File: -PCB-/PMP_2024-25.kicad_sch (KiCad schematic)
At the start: 45 parts, among them J1 OUT, J2 5V, J3 GND, J4 CALIB, Q1 NPN 2N3904, Q2 NPN 2N3904, Q3 NPN MPSA42, Q4 NPN 2N3904

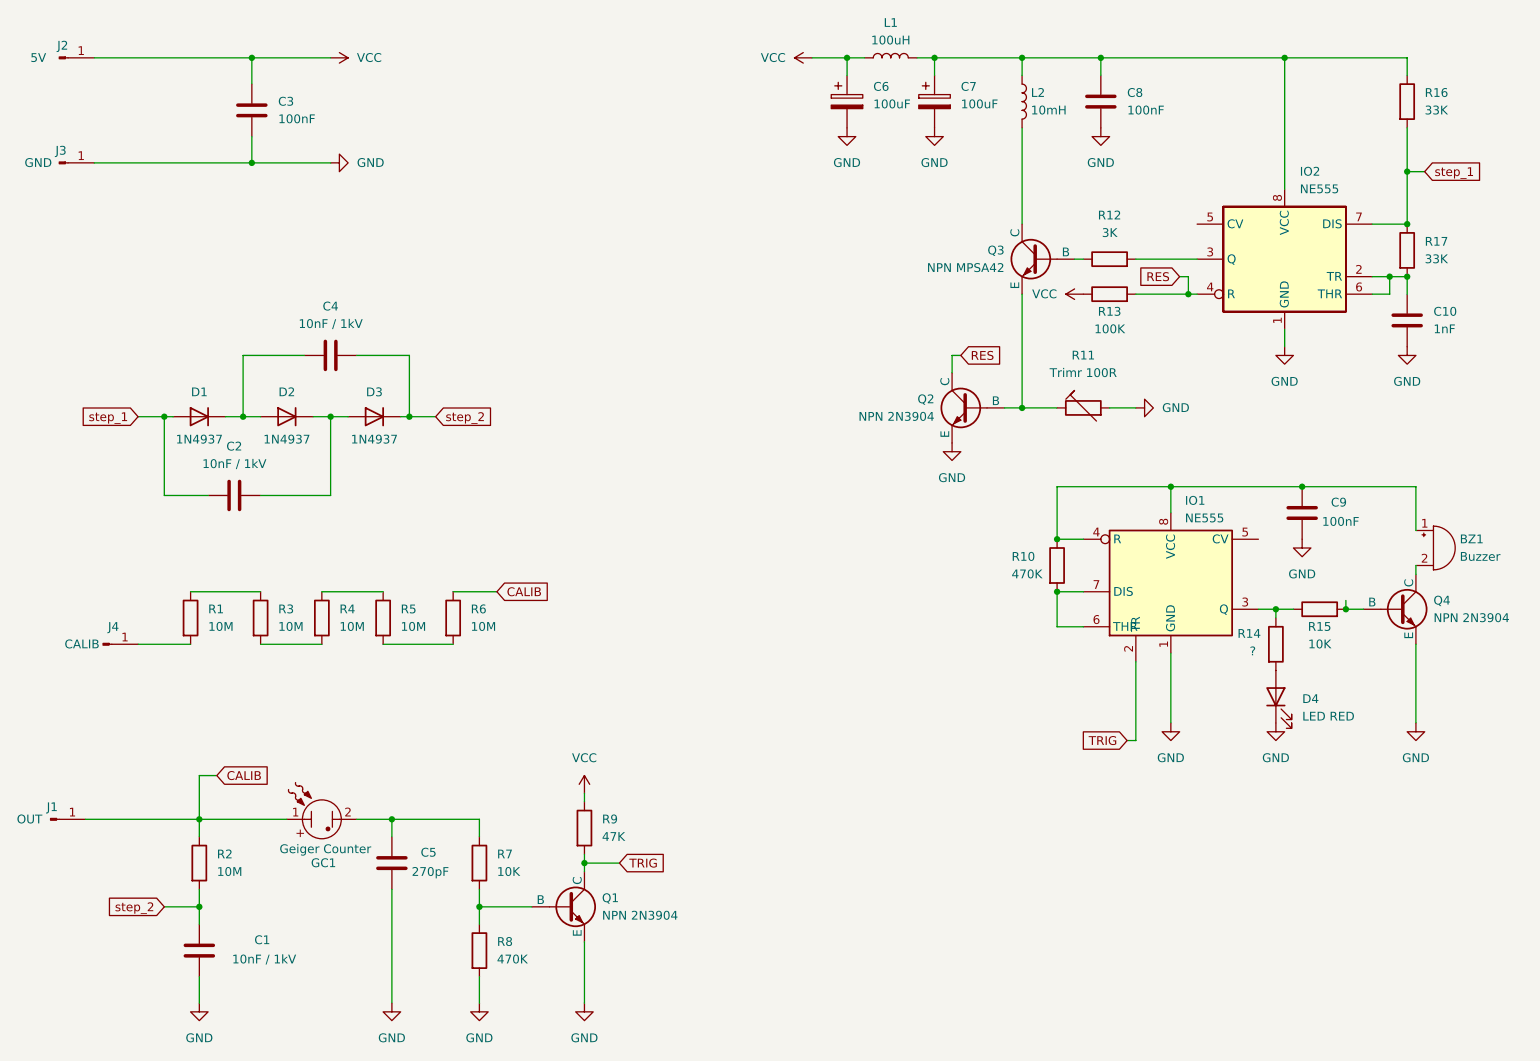
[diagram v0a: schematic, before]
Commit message: schematic update
odebrany chyby, pridany krizky apod
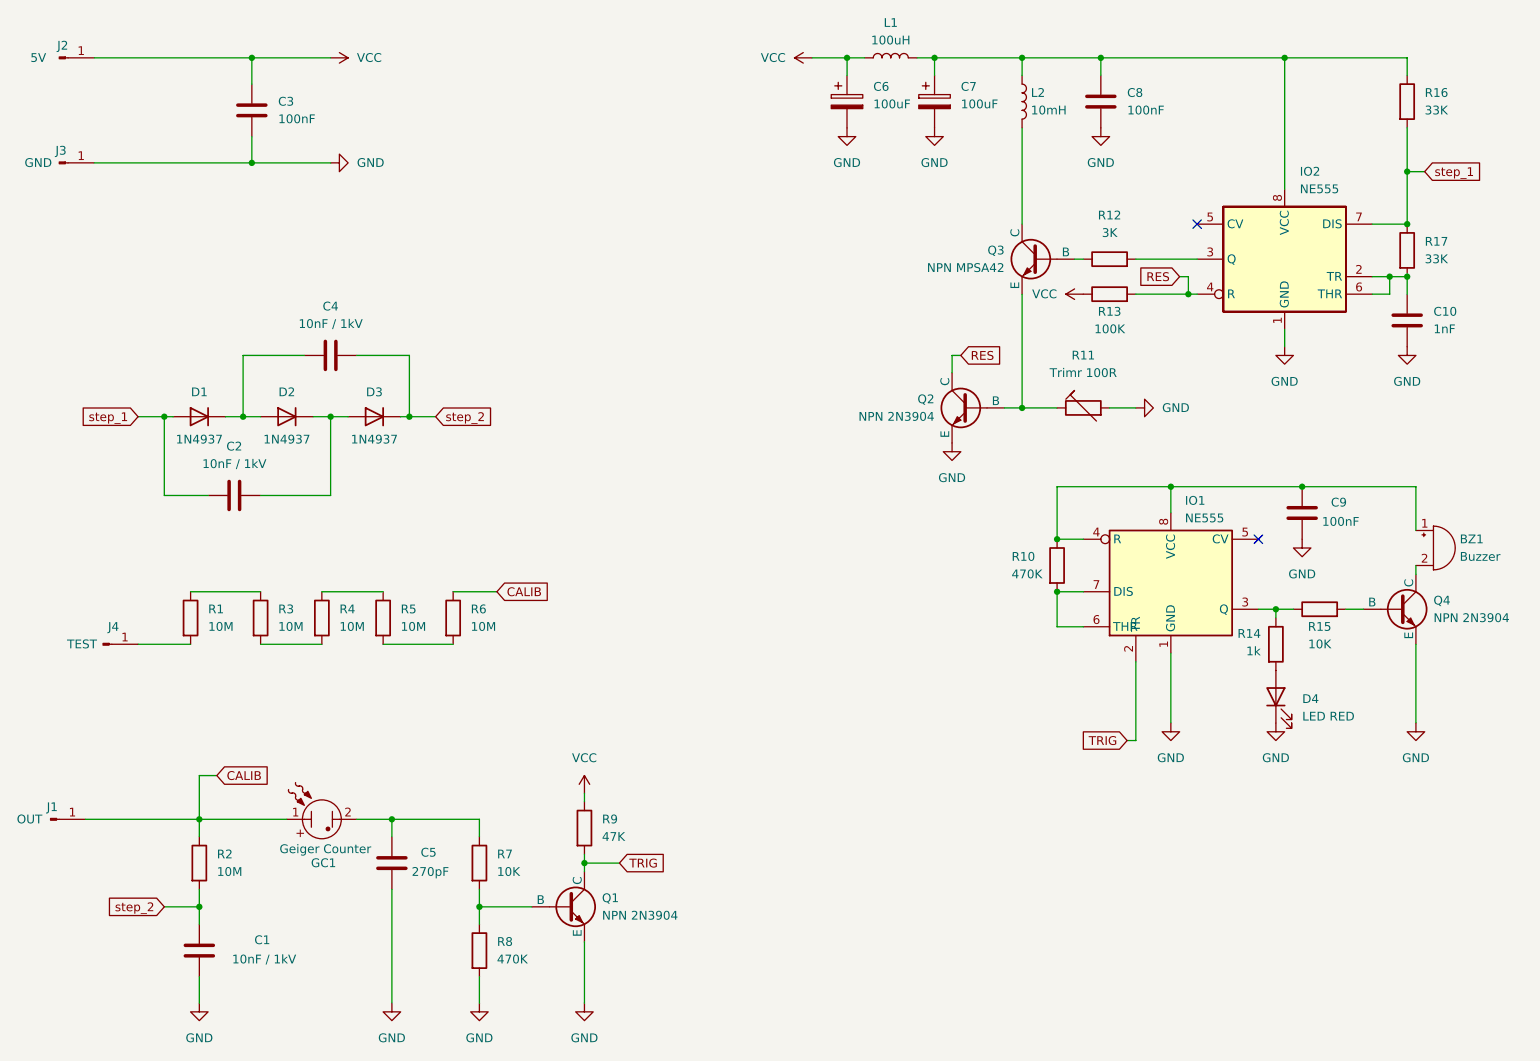
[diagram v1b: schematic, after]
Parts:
- J4: value CALIB -> TEST
- R14: value ? -> 1k
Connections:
- no-connect marks 0 -> 2
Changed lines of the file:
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@@
 	)
 	(junction
-		(at 210.82 104.14)
-		(diameter 0)
-		(color 0 0 0 0)
-	)
-	(junction
 		(at 217.17 55.88)
 		(diameter 0)
@@
 		(color 0 0 0 0)
 	)
+	(no_connect
+		(at 198.12 93.98)
+	)
+	(no_connect
+		(at 189.23 48.26)
+	)
 	(wire
 		(pts
@@
 	(wire
 		(pts
-			(xy 210.82 104.14) (xy 210.82 102.87)
-		)
-		(stroke
-			(width 0)
-			(type default)
-		)
-	)
-	(wire
-		(pts
 			(xy 74.93 76.2) (xy 78.74 76.2)
 		)
@@
 			)
 		)
-		(property "Value" "CALIB "
+		(property "Value" "TEST"
 			(at 27.432 109.22 0)
 			(effects
@@
 			)
 		)
-		(property "Value" "?"
-			(at 196.85 110.236 0)
+		(property "Value" "1k"
+			(at 196.342 110.236 0)
 			(effects
 				(font

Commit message: PCB update
V2
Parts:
- removed R11: Trimr 100R, Resistor_THT:R_Axial_DIN0207_L6.3mm_D2.5mm_P10.16mm_Horizontal, symbol Device:R_Trim
- added R11: Trimr 100R, Potentiometer_THT:Potentiometer_Bourns_3266W_Vertical, symbol Device:R_Potentiometer_Trim
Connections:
- net GND: now also R11.2, R11.3
- net at Q2.2 (B), Q3.3 (E): now also R11.1
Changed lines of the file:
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@@
+	)
+	(symbol
+		(lib_id "Device:R_Potentiometer_Trim")
+		(at 172.72 74.93 90)
+		(unit 1)
+		(exclude_from_sim no)
+		(in_bom yes)
+		(on_board yes)
+		(dnp no)
+		(fields_autoplaced yes)
+		(property "Reference" "R11"
+			(at 172.72 78.74 90)
+			(effects
+				(font
+					(size 1.27 1.27)
+				)
+			)
+		)
+		(property "Value" "Trimr 100R"
+			(at 172.72 81.28 90)
+			(effects
+				(font
+					(size 1.27 1.27)
+				)
+			)
+		)
+		(property "Footprint" "Potentiometer_THT:Potentiometer_Bourns_3266W_Vertical"
+			(at 172.72 74.93 0)
+			(effects
+				(font
+					(size 1.27 1.27)
+				)
+				(hide yes)
+			)
+		)
+		(property "Datasheet" "~"
+			(at 172.72 74.93 0)
+			(effects
+				(font
+					(size 1.27 1.27)
+				)
+				(hide yes)
+			)
+		)
+		(property "Description" "Trim-potentiometer"
+			(at 172.72 74.93 0)
+			(effects
+				(font
+					(size 1.27 1.27)
+				)
+				(hide yes)
+			)
+		)
+		(pin "2"
+		)
+		(pin "3"
+		)
+		(pin "1"
+		)
+		(instances
+			(project "PMP_2024-25"
+				(path "/263df7bf-97e4-4c30-9039-e3f9743ceae4"
+					(reference "R11")
+					(unit 1)
+				)
+			)
+		)
 	)
 	(symbol
@@
 	(symbol
 		(lib_id "power:GND")
+		(at 172.72 71.12 180)
+		(unit 1)
+		(exclude_from_sim no)
+		(in_bom yes)
+		(on_board yes)
+		(dnp no)
+		(property "Reference" "#PWR021"
+			(at 172.72 64.77 0)
+			(effects
+				(font
+					(size 1.27 1.27)
+				)
+				(hide yes)
+			)
+		)
+		(property "Value" "GND"
+			(at 172.72 67.056 0)
+			(effects
+				(font
+					(size 1.27 1.27)
+				)
+			)
+		)
+		(property "Footprint" ""
+			(at 172.72 71.12 0)
+			(effects
+				(font
+					(size 1.27 1.27)
+				)
+				(hide yes)
+			)
+		)
+		(property "Datasheet" ""
+			(at 172.72 71.12 0)
+			(effects
+				(font
+					(size 1.27 1.27)
+				)
+				(hide yes)
+			)
+		)
+		(property "Description" "Power symbol creates a global label with name \"GND\" , ground"
+			(at 172.72 71.12 0)
+			(effects
+				(font
+					(size 1.27 1.27)
+				)
+				(hide yes)
+			)
+		)
+		(pin "1"
+		)
+		(instances
+			(project "PMP_2024-25"
+				(path "/263df7bf-97e4-4c30-9039-e3f9743ceae4"
+					(reference "#PWR021")
+					(unit 1)
+				)
+			)
+		)
+	)
+	(symbol
+		(lib_id "power:GND")
 		(at 72.39 161.29 0)
 		(unit 1)
@@
 					(unit 1)
 				)
-			)
-		)
-	)
-	(symbol
-		(lib_id "Device:R_Trim")
-		(at 172.72 74.93 90)
-		(unit 1)
-		(exclude_from_sim no)
-		(in_bom yes)
-		(on_board yes)
-		(dnp no)
-		(fields_autoplaced yes)
-		(property "Reference" "R11"
-			(at 172.72 67.31 90)
-			(effects
-				(font
-					(size 1.27 1.27)
-				)
-			)
-		)
-		(property "Value" "Trimr 100R"
-			(at 172.72 69.85 90)
-			(effects
-				(font
-					(size 1.27 1.27)
-				)
-			)
-		)
-		(property "Footprint" "Resistor_THT:R_Axial_DIN0207_L6.3mm_D2.5mm_P10.16mm_Horizontal"
-			(at 172.72 76.708 90)
-			(effects
-				(font
-					(size 1.27 1.27)
-				)
-				(hide yes)
-			)
-		)
-		(property "Datasheet" "~"
-			(at 172.72 74.93 0)
-			(effects
-				(font
-					(size 1.27 1.27)
-				)
-				(hide yes)
-			)
-		)
-		(property "Description" "Trimmable resistor (preset resistor)"
-			(at 172.72 74.93 0)
-			(effects
-				(font
-					(size 1.27 1.27)
-				)
-				(hide yes)
-			)
-		)
-		(pin "1"
-		)
-		(pin "2"
-		)
-		(instances
-			(project "PMP_2024-25"
-				(path "/263df7bf-97e4-4c30-9039-e3f9743ceae4"
-					(reference "R11")
-					(unit 1)
-				)

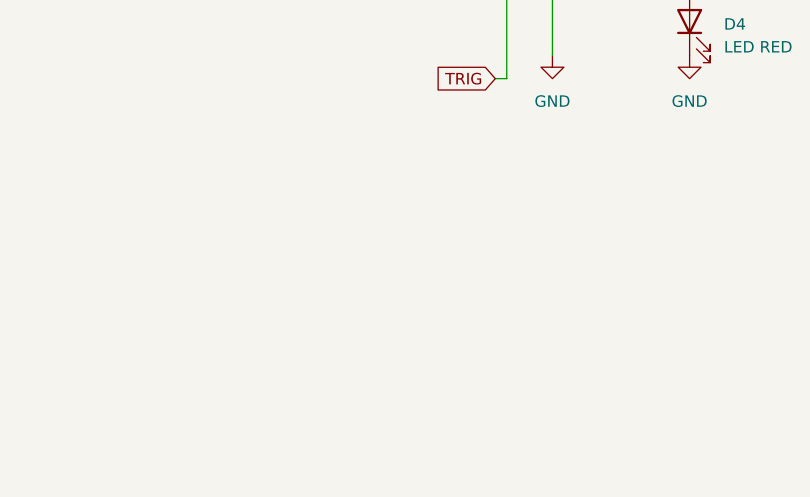
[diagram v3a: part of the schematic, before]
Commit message: added image on PCB
PDF prints added too
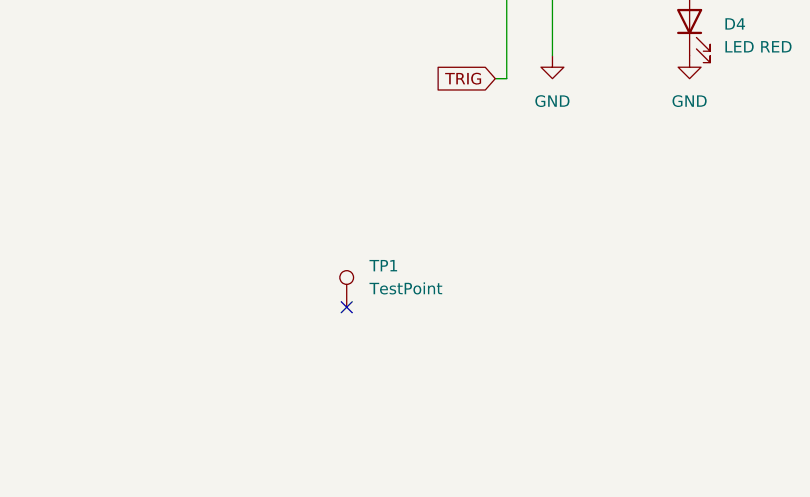
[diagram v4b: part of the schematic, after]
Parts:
- added TP1: TestPoint, graphics:obrazek1, symbol Connector:TestPoint
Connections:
- no-connect marks 2 -> 3
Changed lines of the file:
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@@
 	)
 	(no_connect
+		(at 162.56 148.59)
+	)
+	(no_connect
 		(at 198.12 93.98)
 	)
@@
 					(unit 1)
 				)
+			)
+		)
+	)
+	(symbol
+		(lib_id "Connector:TestPoint")
+		(at 162.56 148.59 0)
+		(unit 1)
+		(exclude_from_sim no)
+		(in_bom yes)
+		(on_board yes)
+		(dnp no)
+		(fields_autoplaced yes)
+		(property "Reference" "TP1"
+			(at 165.1 144.0179 0)
+			(effects
+				(font
+					(size 1.27 1.27)
+				)
+				(justify left)
+			)
+		)
+		(property "Value" "TestPoint"
+			(at 165.1 146.5579 0)
+			(effects
+				(font
+					(size 1.27 1.27)
+				)
+				(justify left)
+			)
+		)
+		(property "Footprint" "graphics:obrazek1"
+			(at 167.64 148.59 0)
+			(effects
+				(font
+					(size 1.27 1.27)
+				)
+				(hide yes)
+			)
+		)
+		(property "Datasheet" "~"
+			(at 167.64 148.59 0)
+			(effects
+				(font
+					(size 1.27 1.27)
+				)
+				(hide yes)
+			)
+		)
+		(property "Description" "test point"
+			(at 162.56 148.59 0)
+			(effects
+				(font
+					(size 1.27 1.27)
+				)
+				(hide yes)
+			)
+		)
+		(pin "1"
+		)
+		(instances
+			(project "PMP_2024-25"
+				(path "/263df7bf-97e4-4c30-9039-e3f9743ceae4"
+					(reference "TP1")
+					(unit 1)
+				)

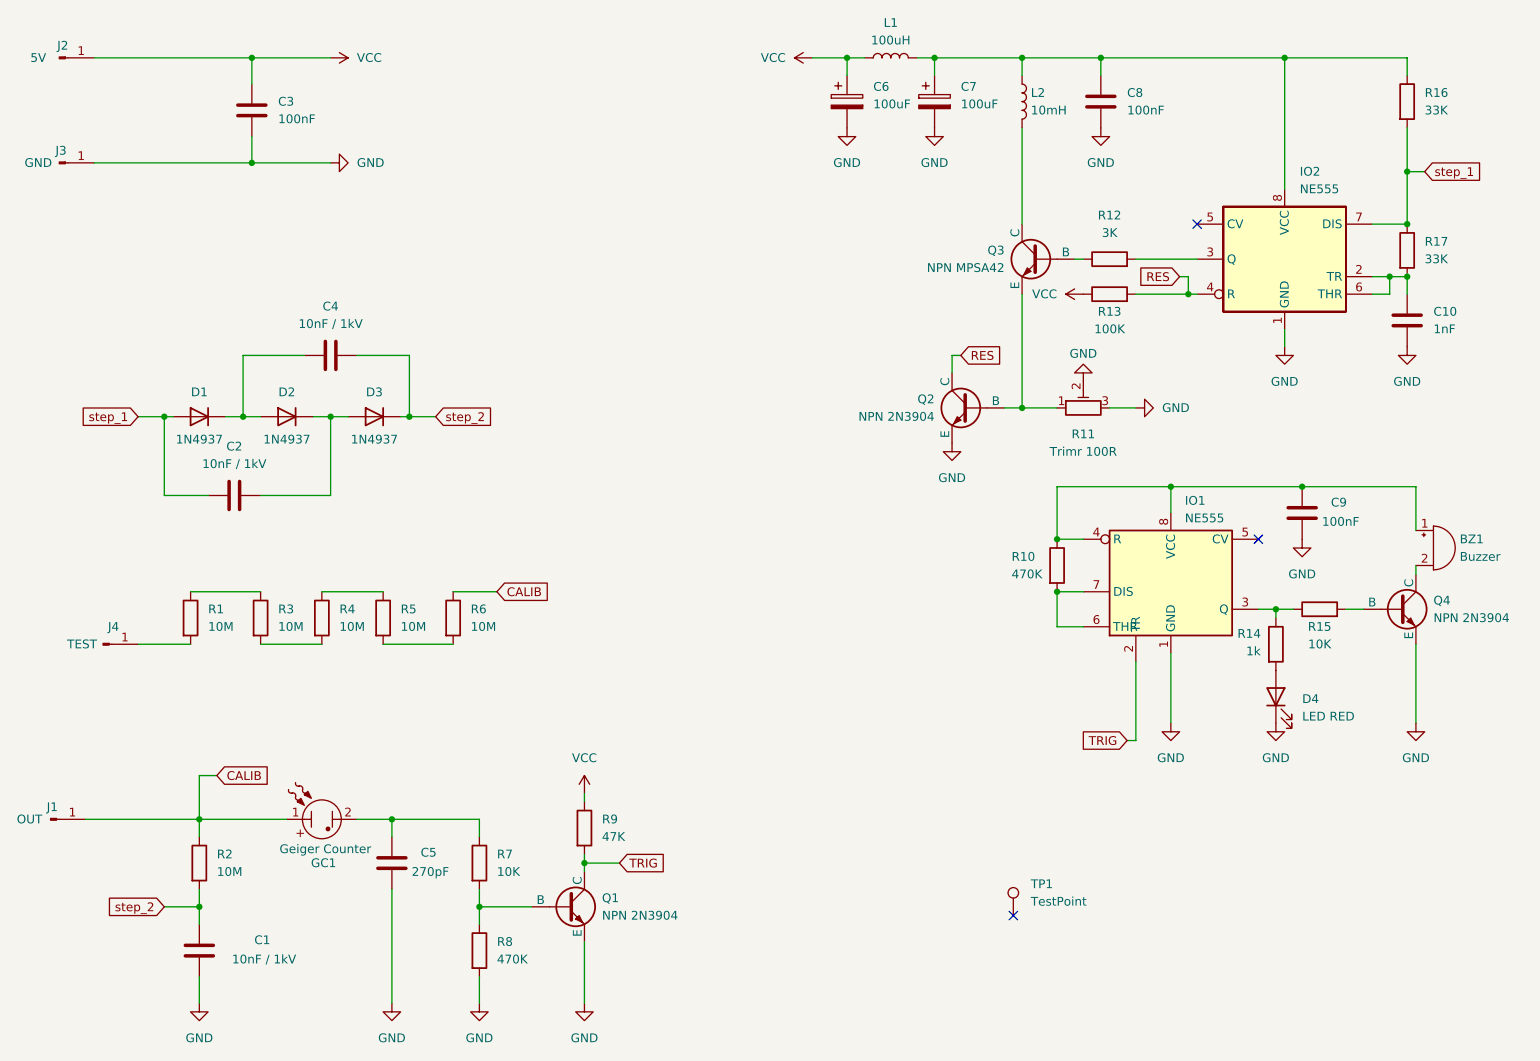
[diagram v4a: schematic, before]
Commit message: EDITS ON CHEMATIC AND PCB
renamed pins and changed positions
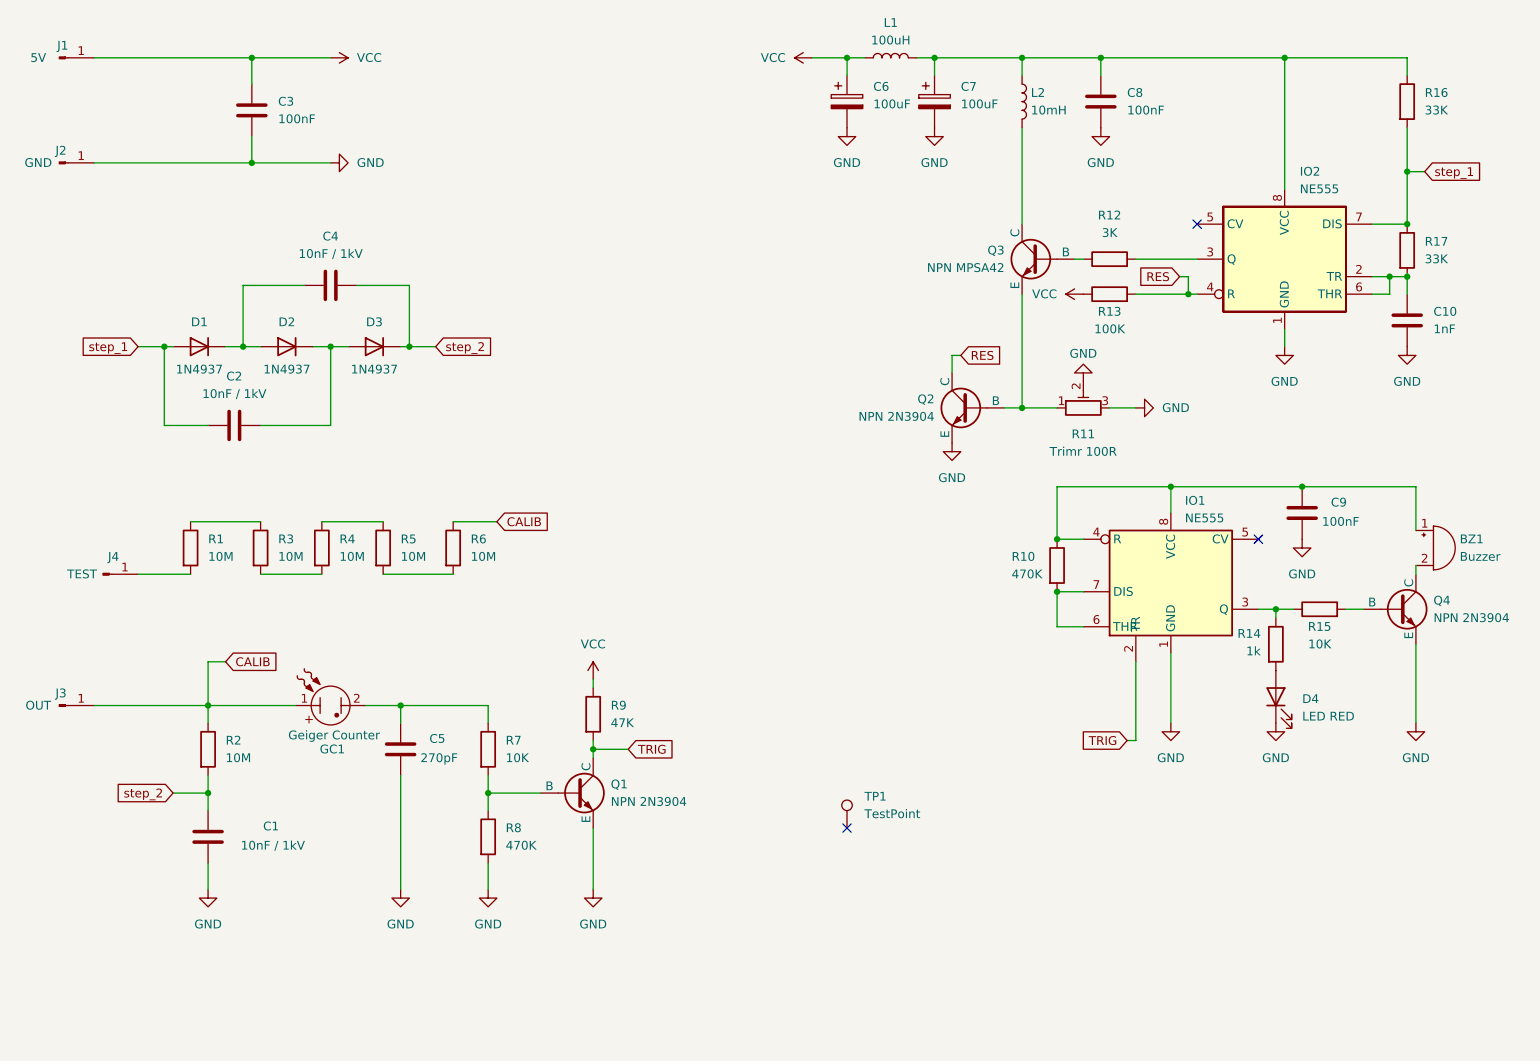
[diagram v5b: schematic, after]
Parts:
- renumbered J2 to J1, J3 to J2, J1 to J3
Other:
- moved on the sheet: C1, C2, C4, C5, D1, D2, D3, GC1, J3, J4, Q1, R1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

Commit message: edits on pcb, design etc.
box model soon, tommorow creating pcb v2
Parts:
- R11: footprint Potentiometer_THT:Potentiometer_Bourns_3266W_Vertical -> Potentiometer_THT:Potentiometer_Bourns_3296W_Vertical
- TP1: value TestPoint -> obrazek 1
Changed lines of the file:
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@@
 			)
 		)
-		(property "Footprint" "Potentiometer_THT:Potentiometer_Bourns_3266W_Vertical"
+		(property "Footprint" "Potentiometer_THT:Potentiometer_Bourns_3296W_Vertical"
 			(at 172.72 74.93 0)
 			(effects
@@
 			)
 		)
-		(property "Value" "TestPoint"
+		(property "Value" "obrazek 1"
 			(at 140.97 133.8579 0)
 			(effects
